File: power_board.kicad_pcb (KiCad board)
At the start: 2 copper layers, 141 x 90 mm, 172 parts, among them CON1 MICROUSB, J1 Conn_02x03_Odd_Even, J10 Conn_01x02, J11 Conn_01x02, J12 Conn_01x02, J13 Conn_01x02, J14 Conn_01x02, J15 Conn_01x02, J16 Conn_01x02, J17 Conn_01x02, J18 Conn_01x02, J19 Conn_01x02, J2 Conn_01x01, J20 Conn_01x02, J21 Conn_01x03, J22 Conn_01x03, J23 Conn_01x03, J24 Conn_01x03, J25 Conn_01x03, J26 Conn_01x02, J27 Conn_01x02, J28 Conn_01x02, J29 Conn_01x02, J3 Conn_01x01, J30 Conn_01x02, J31 Conn_01x02, J32 Conn_01x02, J33 Conn_01x02, J4 Conn_01x01, J5 ATX-24, J6 Conn_01x02, J7 Conn_01x02, J8 Conn_01x02, J9 Conn_01x02, K1 lsts-devices:RELAY_1RT, K2 lsts-devices:RELAY_1RT, K3 lsts-devices:RELAY_1RT, K4 lsts-devices:RELAY_1RT, K5 lsts-devices:RELAY_1RT, Q1 MMBT4401-7-F, Q10 MMBT4401-7-F, Q11 SI7113ADN-T1-GE3, Q12 MMBT4401-7-F, Q13 MMBT4401-7-F, Q14 MMBT4401-7-F, Q15 SI7113ADN-T1-GE3, Q16 SI7113ADN-T1-GE3, Q17 SI7113ADN-T1-GE3, Q18 MMBT4401-7-F, Q19 MMBT4401-7-F, Q2 MMBT4401-7-F, Q20 SI7113ADN-T1-GE3, Q21 SI7113ADN-T1-GE3, Q3 MMBT4401-7-F, Q4 SI7113ADN-T1-GE3, Q5 SI7113ADN-T1-GE3, Q6 MMBT4401-7-F, Q7 MMBT4401-7-F, Q8 SI7113ADN-T1-GE3, Q9 SI7113ADN-T1-GE3, SW1 SW_Push, U1 PCA9685PW, U10 DRV8801PWP, U11 DRV8801PWP, U12 DRV8801PWP, U2 ATMEGA328P-AU, U3 PCA9685PW, U4 FT232RL, U5 DRV8801PWP, U6 DRV8801PWP, U7 DRV8801PWP, U8 DRV8801PWP, U9 DRV8801PWP, Y1 Crystal

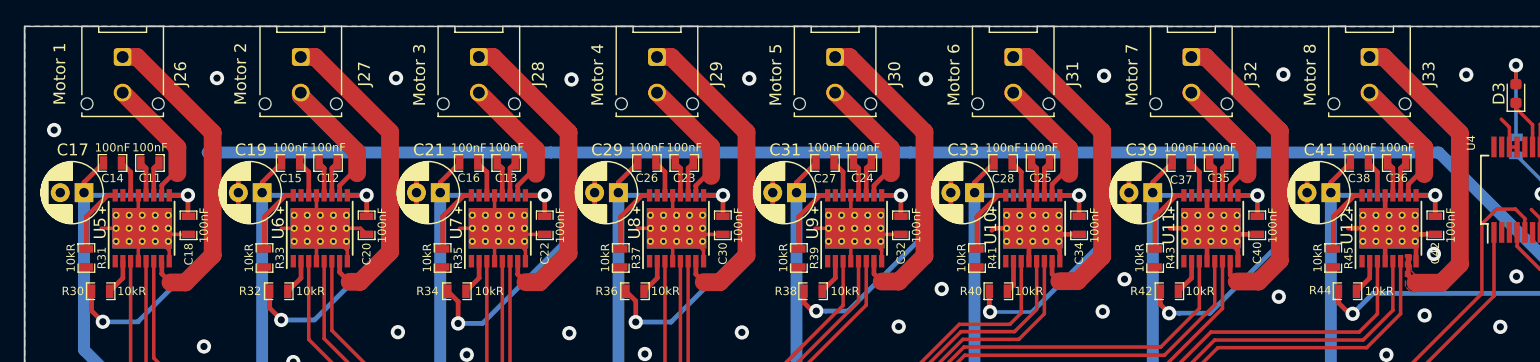
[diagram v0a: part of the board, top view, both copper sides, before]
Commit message: Increased motor connectors distance to board edge
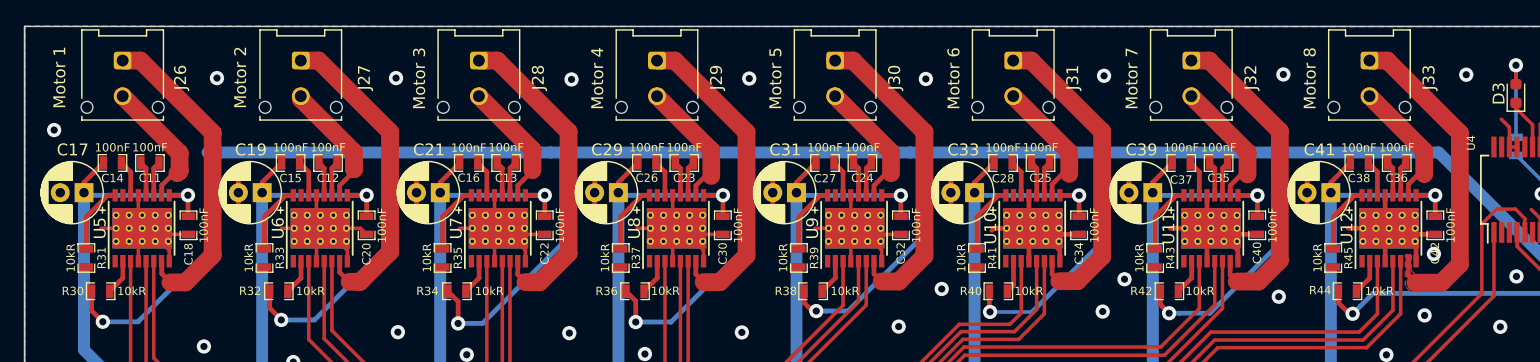
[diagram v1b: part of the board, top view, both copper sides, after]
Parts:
- moved J26 0.30 mm to (88.3, 62.9)
- moved J27 0.30 mm to (103.3, 62.9)
- moved J28 0.30 mm to (118.3, 62.9)
- moved J29 0.30 mm to (133.3, 62.9)
- moved J30 0.30 mm to (148.3, 62.9)
- moved J31 0.30 mm to (163.3, 62.9)
- moved J32 0.30 mm to (178.3, 62.9)
- moved J33 0.30 mm to (193.3, 62.9)
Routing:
- net Net-(J27-Pad2): track 11.5 -> 10.7 mm
- net Net-(J28-Pad2): track 11.6 -> 10.9 mm

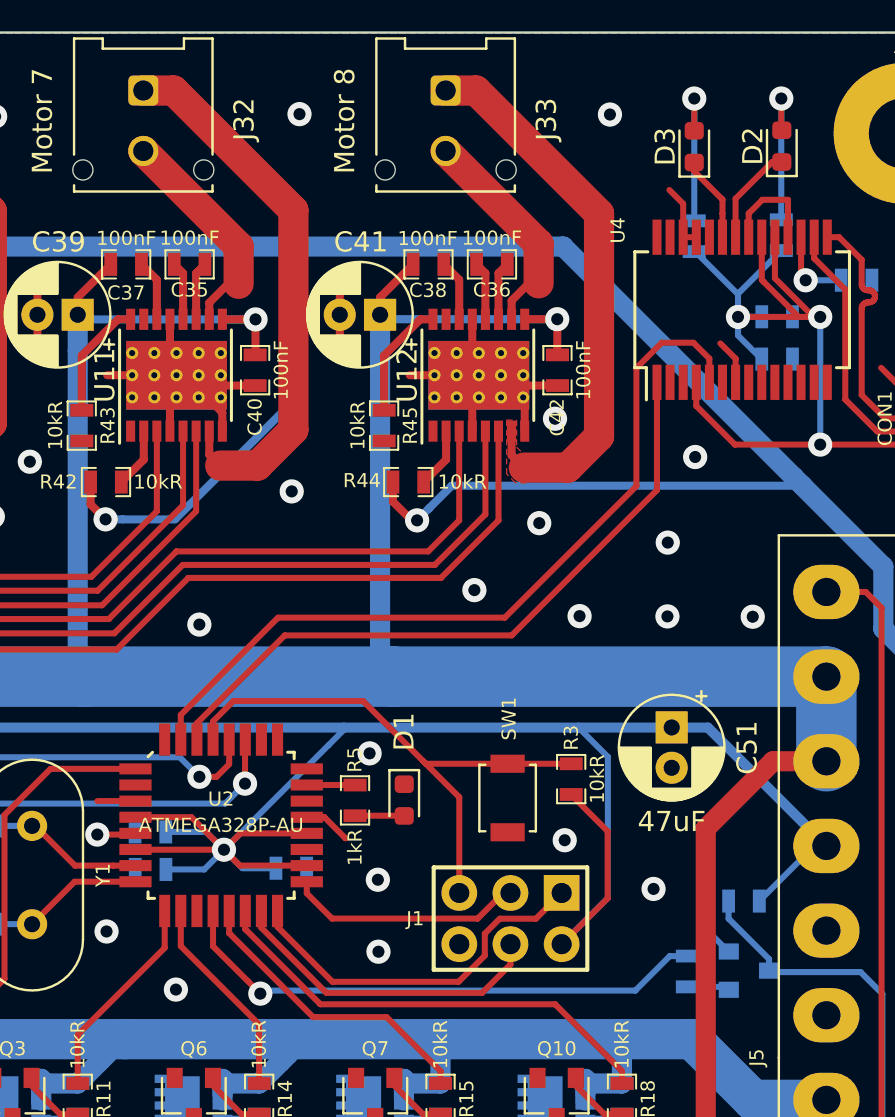
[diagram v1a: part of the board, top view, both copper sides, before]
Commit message: Reroute ISP
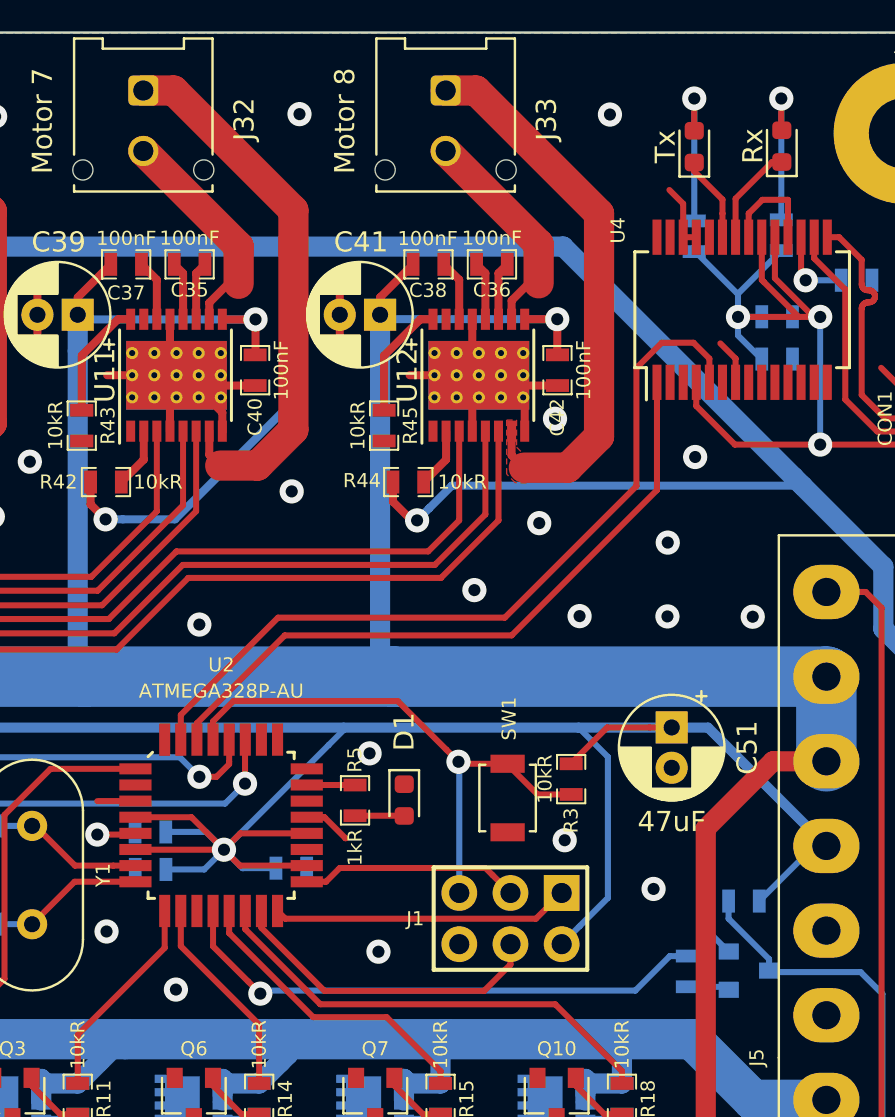
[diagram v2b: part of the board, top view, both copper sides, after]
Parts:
- turned R3 to 270 degrees
- renumbered D2 to Rx, D3 to Tx
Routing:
- net /MISO: track 18.5 -> 14.8 mm
- net /+5V_SB: track 207.5 -> 204.1 mm
- net /SCK: track 11.7 -> 10.9 mm
- net /RESET: vias 0 -> 1
- net GND: vias 94 -> 93

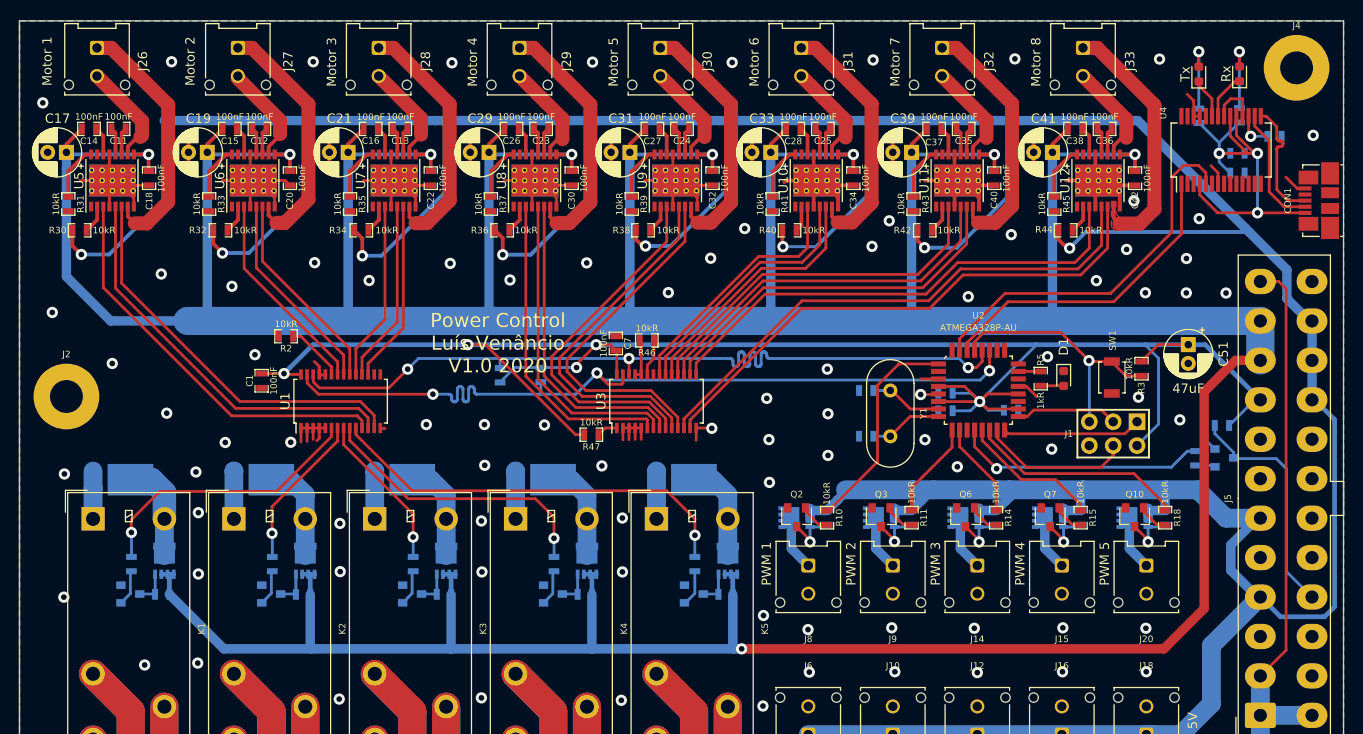
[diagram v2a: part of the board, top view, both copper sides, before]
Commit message: Increased motor connectors distance to board edge
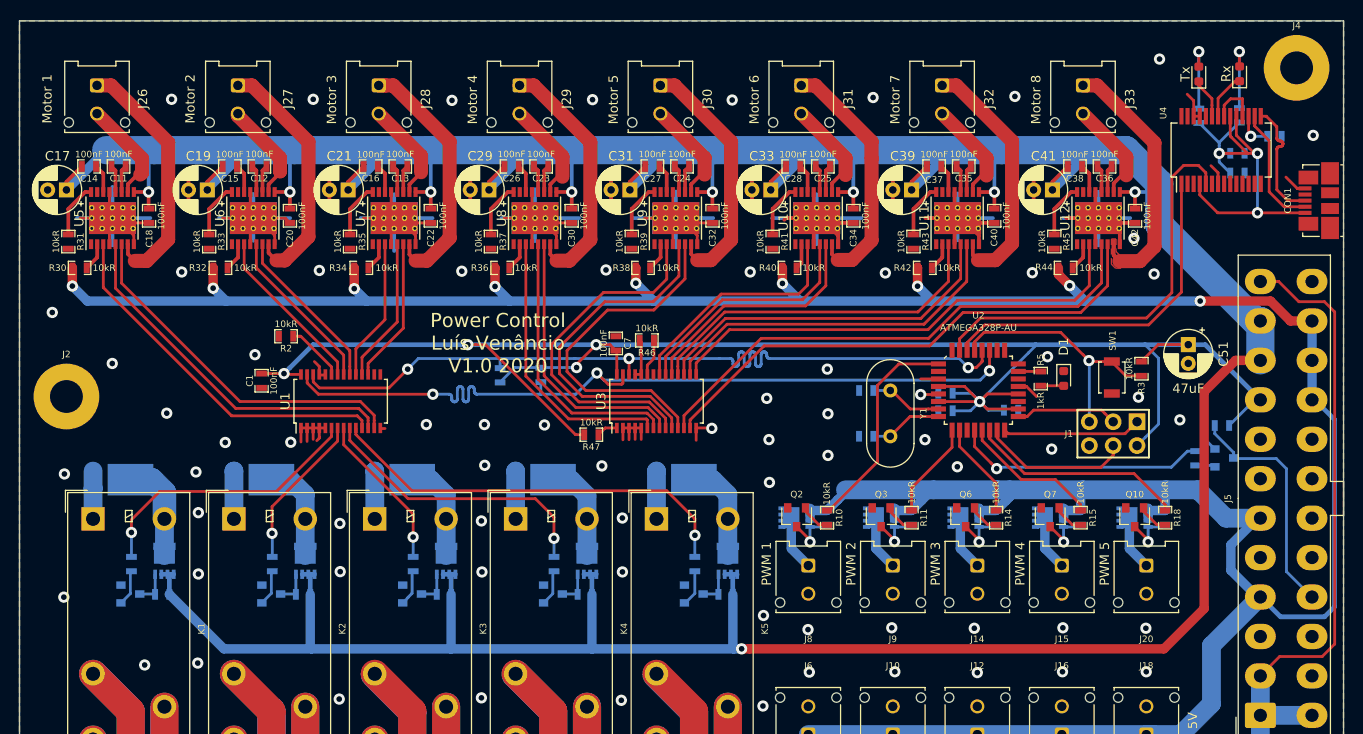
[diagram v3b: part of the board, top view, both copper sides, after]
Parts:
- moved C11 4.00 mm to (90.5, 75.5)
- moved C12 4.00 mm to (105.5, 75.5)
- moved C13 4.00 mm to (120.5, 75.5)
- moved C14 4.00 mm to (87.4, 75.5)
- moved C15 4.00 mm to (102.4, 75.5)
- moved C16 4.00 mm to (117.4, 75.5)
- moved C17 4.00 mm to (85.0, 78.0)
- moved C18 4.00 mm to (93.8, 80.8)
- moved C19 4.00 mm to (100.0, 78.0)
- moved C20 4.00 mm to (108.8, 80.8)
- moved C21 4.00 mm to (115.0, 78.0)
- moved C22 4.00 mm to (123.8, 80.8)
- moved C23 4.00 mm to (135.6, 75.5)
- moved C24 4.00 mm to (150.6, 75.5)
- moved C25 4.00 mm to (165.6, 75.5)
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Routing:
- net +5V: track 493.6 -> 349.1 mm, vias 8 -> 9
- net +12V: track 583.3 -> 457.9 mm
- net GND: track 234.5 -> 342.9 mm, vias 93 -> 79
- net +3V3: track 109.5 -> 118.1 mm
- net /MTR2_EN: track 21.8 -> 17.7 mm
- net /MTR4_SL: track 33.4 -> 29.4 mm
- net /MTR4_PH: track 33.8 -> 29.8 mm
- net /MTR3_SL: track 19.5 -> 15.5 mm
- net /MTR3_PH: track 19.2 -> 15.2 mm
- net /MTR3_EN: track 19.5 -> 15.5 mm
- net /MTR2_SL: track 21.8 -> 17.8 mm
- net /MTR2_PH: track 22.1 -> 18.1 mm
- net /MTR1_PH: track 42.9 -> 38.9 mm
- net /MTR1_EN: track 42.3 -> 38.3 mm
- net /MTR4_EN: track 33.2 -> 29.2 mm
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
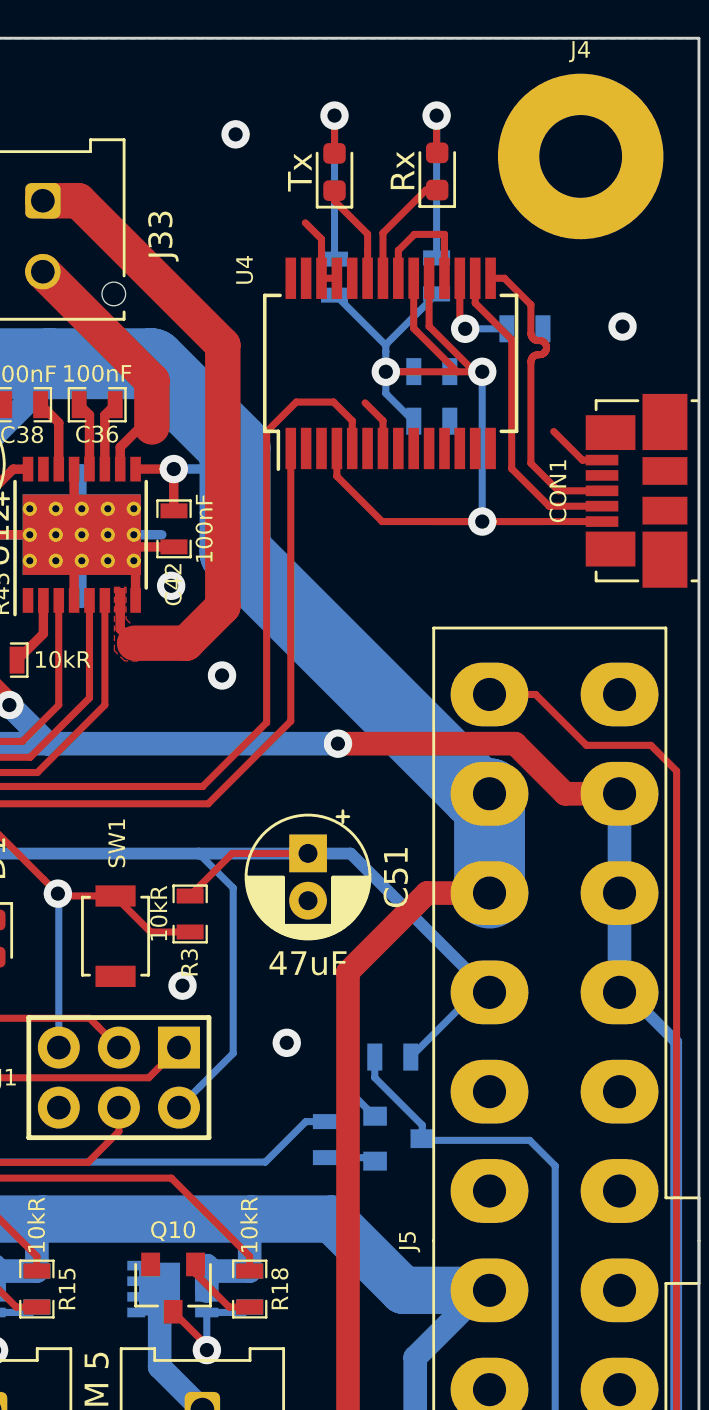
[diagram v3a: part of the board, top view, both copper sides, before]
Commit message: Changed ATX-24 symbol to merged version.
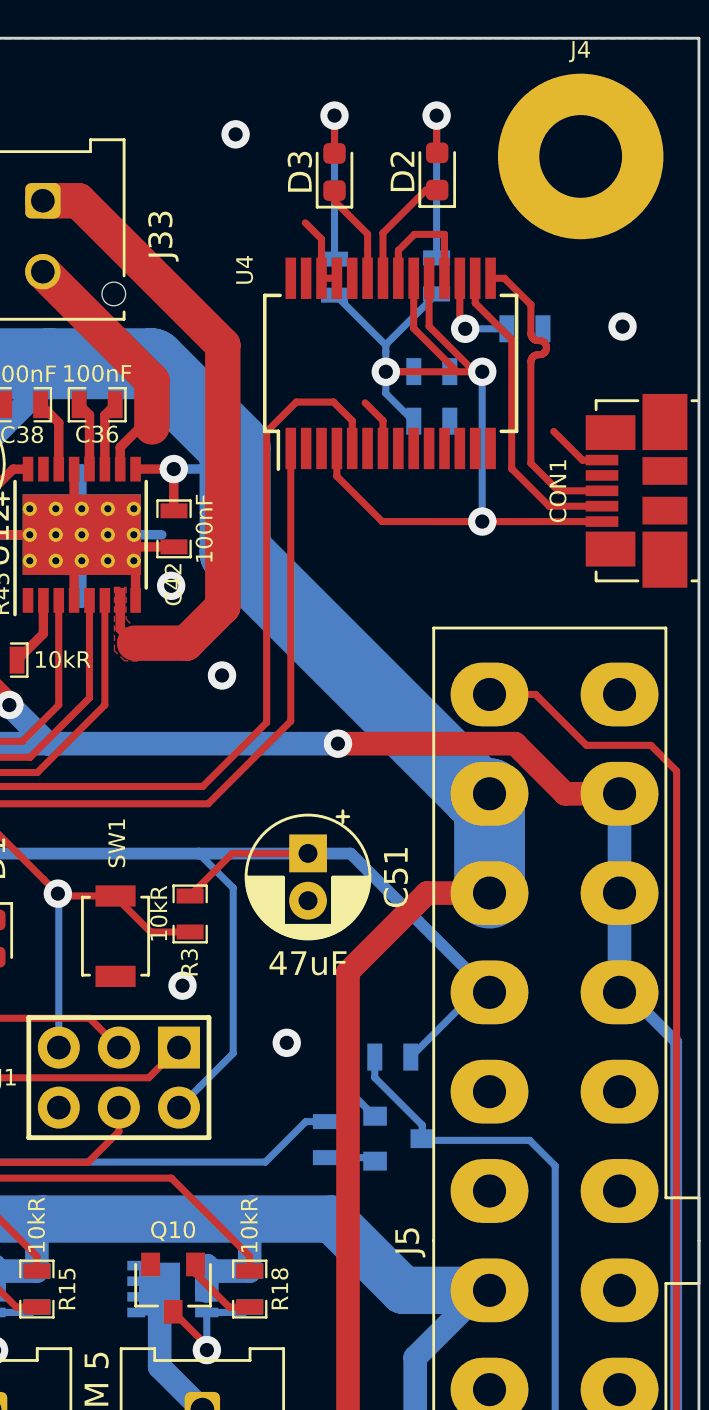
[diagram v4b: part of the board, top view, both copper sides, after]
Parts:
- renumbered Rx to D2, Tx to D3

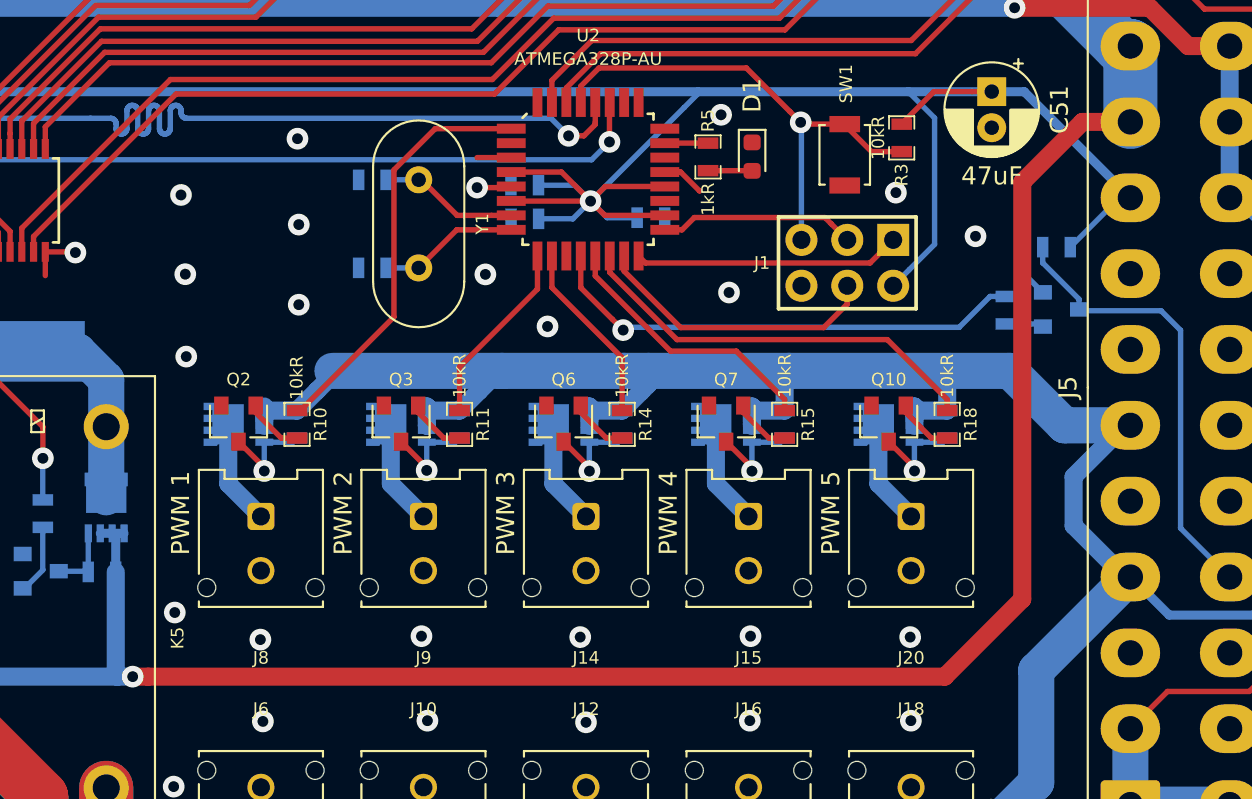
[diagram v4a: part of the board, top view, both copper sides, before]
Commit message: Switch PMW 1 & 2 to 12V
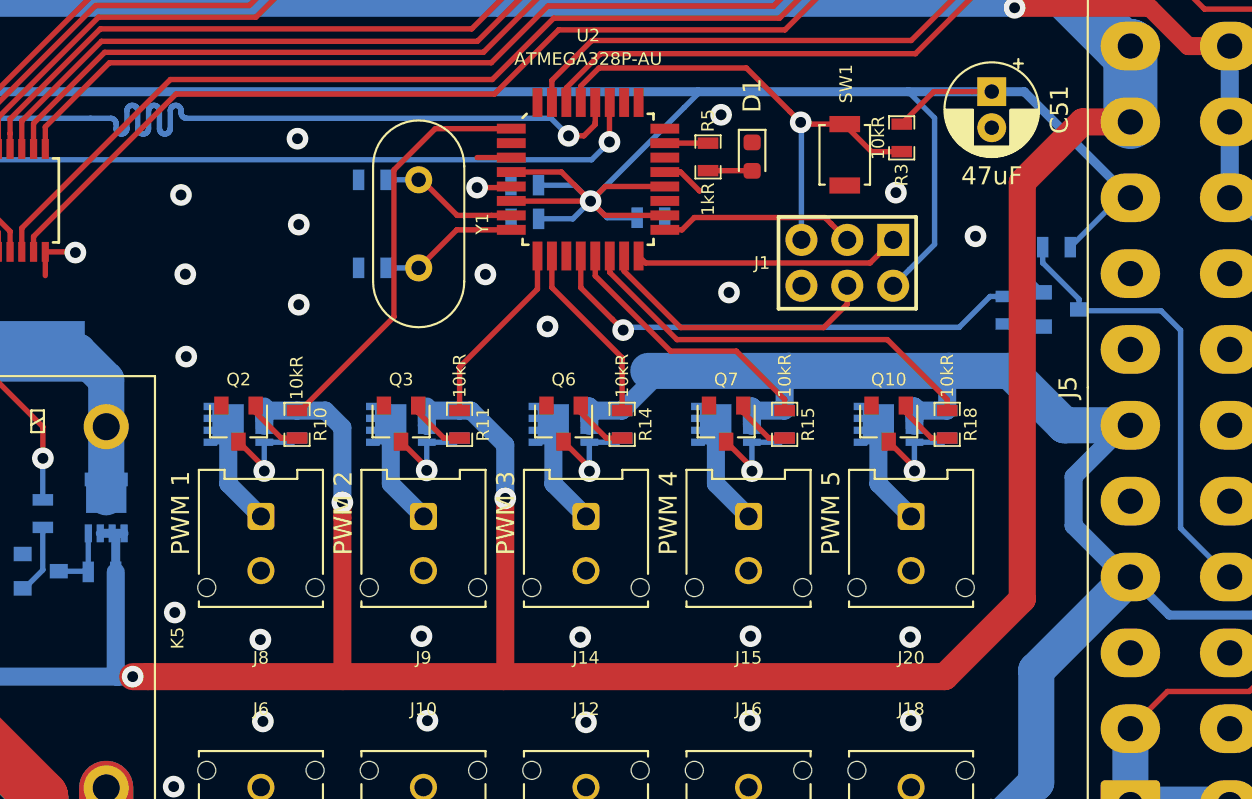
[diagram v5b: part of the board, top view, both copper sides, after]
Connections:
- Q4 pad S: +5V -> +12V
- Q5 pad S: +5V -> +12V
- R12 pad 2: +5V -> +12V
- R13 pad 2: +5V -> +12V
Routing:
- net +12V: track 457.9 -> 495.9 mm, vias 9 -> 11
- net +5V: track 349.1 -> 319.9 mm
